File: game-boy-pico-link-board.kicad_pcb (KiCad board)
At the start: 2 copper layers, 83 x 26 mm, 6 parts, among them J1 GBA_Link, J2 GB_Link, J3 Breakout, SW1 SW_SPDT, U1 Pico, U2 BOB-12009

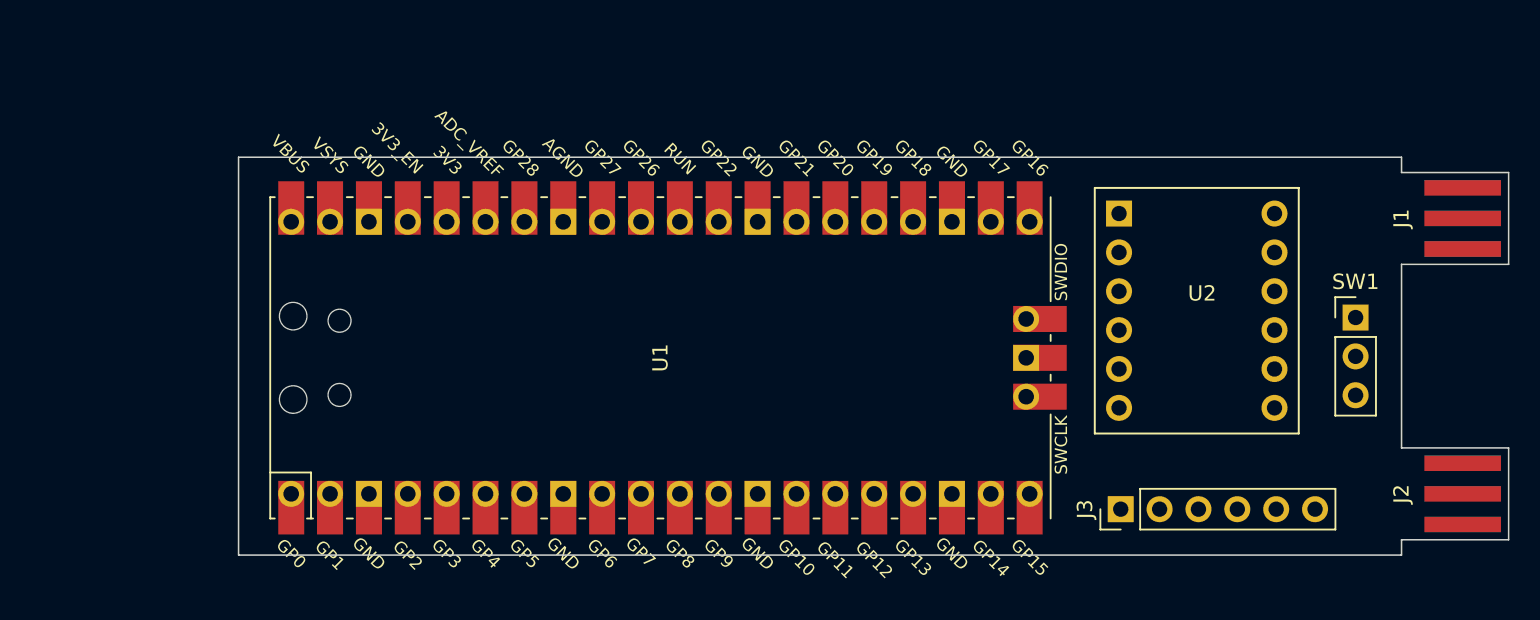
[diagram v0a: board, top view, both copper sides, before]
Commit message: Update Design and Add Routing
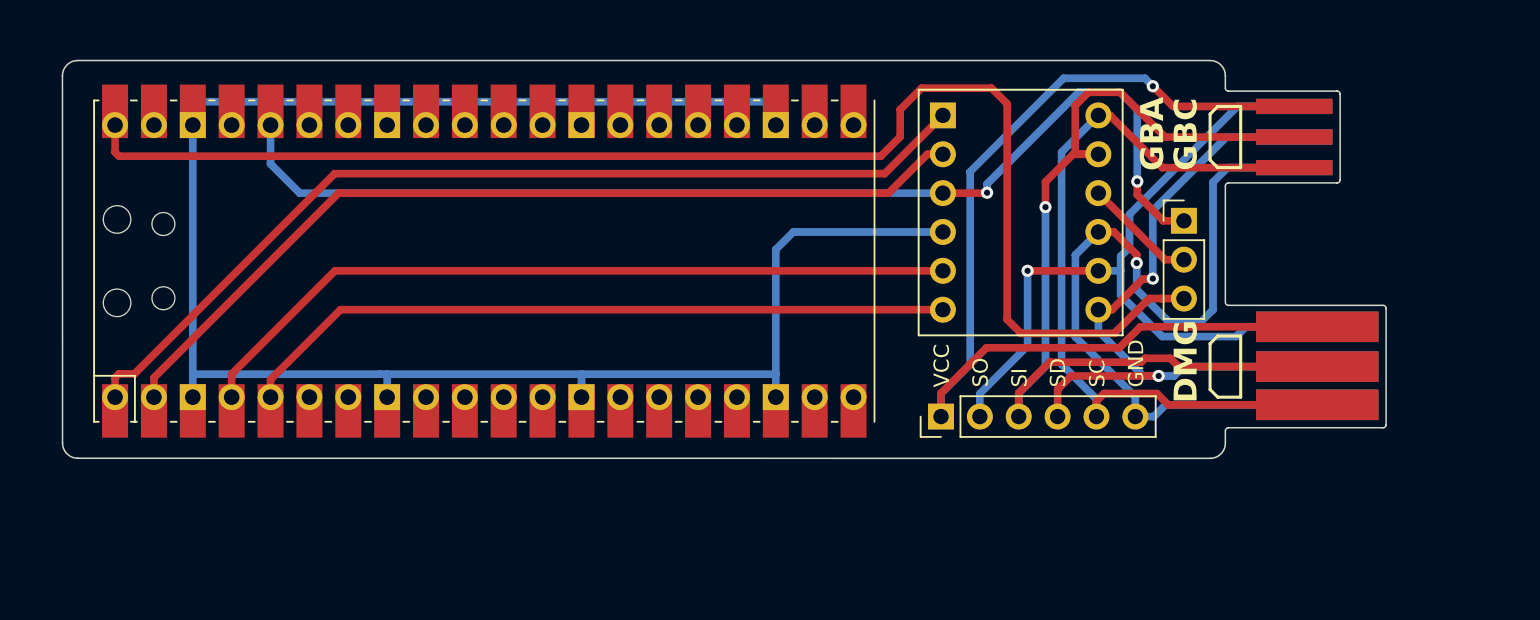
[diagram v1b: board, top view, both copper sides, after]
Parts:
- J1: moved to B.Cu
- J2: value GB_Link -> DMG_Link; footprint gb-link-socket:gb-link-socket -> gb-link-socket:dmg-link-socket; moved to B.Cu
- U1: value Pico -> Pico_Reduced; footprint MCU_RaspberryPi_and_Boards:RPi_Pico_SMD_TH -> MCU_RaspberryPi_and_Boards:RPi_Pico_SMD_TH_REDUCED
- moved J3 13.2 mm to (128.9, 108.0)
- moved U2 13.2 mm to (134.5, 94.6)
- moved U1 13.1 mm to (99.1, 97.8)
- moved SW1 12.9 mm to (144.8, 95.2)
- moved J2 12.6 mm to (153.5, 104.7)
- moved J1 12.2 mm to (152.0, 89.7)
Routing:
- net GND: track 0.00 -> 124.2 mm
- net +5V: track 0.00 -> 90.5 mm
- net +3.3V: track 0.00 -> 72.8 mm, vias 0 -> 2
- net /GBVCC: track 0.00 -> 69.2 mm, vias 0 -> 1
- net /SI: track 0.00 -> 63.0 mm, vias 0 -> 1
- net /PSC: track 0.00 -> 62.5 mm
- net /PSI: track 0.00 -> 58.9 mm
- net GND1: track 0.00 -> 52.2 mm, vias 0 -> 1
- net /SC: track 0.00 -> 51.8 mm
- net /PSO: track 0.00 -> 50.8 mm
- net /SO: track 0.00 -> 50.3 mm, vias 0 -> 1
- net /PSD: track 0.00 -> 47.0 mm
- net /SD: track 0.00 -> 46.0 mm, vias 0 -> 2
- net VCCLOGIC: track 0.00 -> 7.39 mm
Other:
- board size 83 x 26 mm -> 86.5 x 26 mm
- board text added: "DMG"
- board text added: "GBA"
- board text added: "GBC"
- board text added: "GND"
- board text added: "GP0 <-> SC GP1 <-> SI GP2 <-> SO GP3 <-> SD"
- board text added: "SC"
- board text added: "SD"
- board text added: "SI"
- board text added: "SO"
- board text added: "USB TO GAMEBOY LINK CABLE ADAPTER"
- board text added: "VCC"

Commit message: Update Design
Shortened DMG socket
Replace components layout
Add more silkscreen text
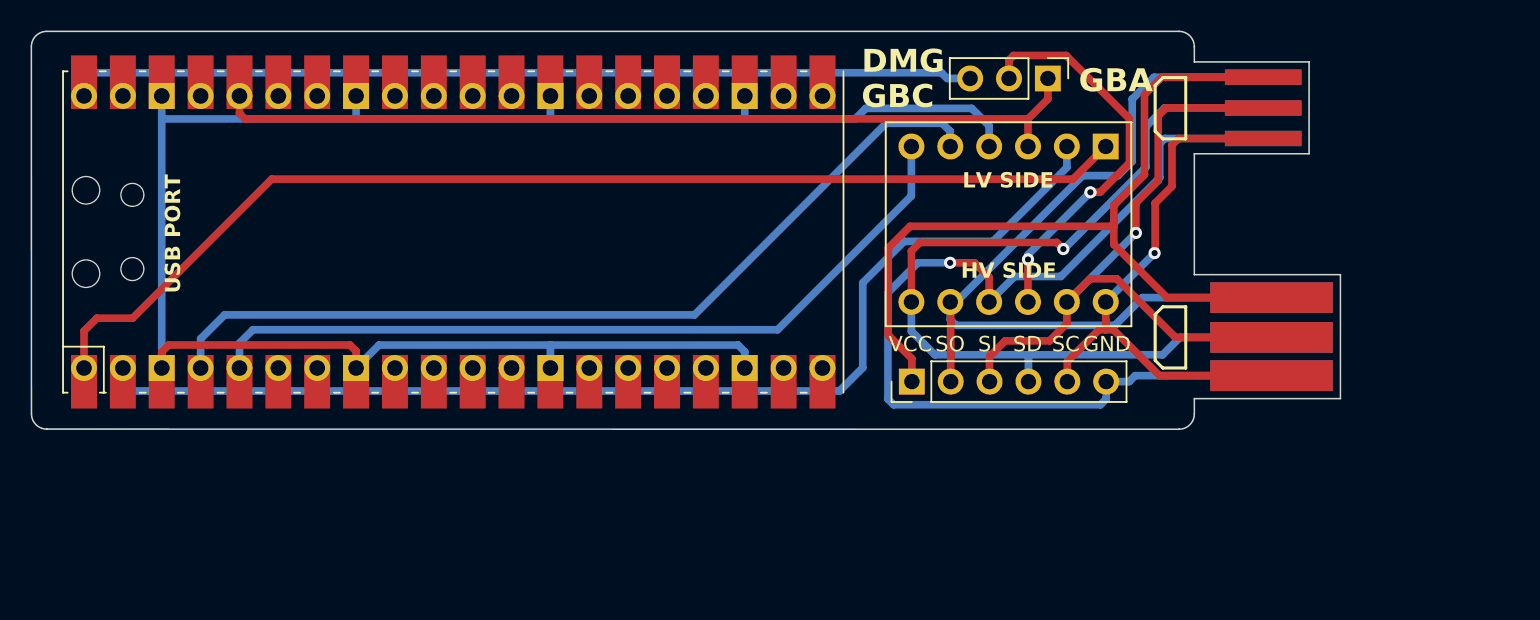
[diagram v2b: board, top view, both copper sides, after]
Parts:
- moved SW1 12.9 mm to (135.9, 85.9), turned to -90 degrees
- moved J2 3.54 mm to (150.5, 102.8)
- moved J3 2.98 mm to (127.0, 105.7)
- moved J1 2.78 mm to (150.0, 87.8)
- moved U1 2.78 mm to (97.0, 95.9)
- moved U2 1.64 mm to (133.3, 95.8), turned to -90 degrees
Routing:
- net +5V: track 90.5 -> 59.4 mm
- net VCCLOGIC: track 7.39 -> 26.0 mm, vias 0 -> 2
- net /SI: track 63.0 -> 46.3 mm
- net +3.3V: track 72.8 -> 57.8 mm, vias 2 -> 0
- net /SC: track 51.8 -> 36.8 mm, vias 0 -> 1
- net /PSI: track 58.9 -> 73.6 mm
- net GND1: track 52.2 -> 66.7 mm
- net /SD: track 46.0 -> 60.4 mm, vias 2 -> 1
- net /GBVCC: track 69.2 -> 55.3 mm, vias 1 -> 0
- net /PSC: track 62.5 -> 74.2 mm
- net /PSO: track 50.8 -> 57.9 mm
- net /SO: track 50.3 -> 57.3 mm, vias 1 -> 0
- net /PSD: track 47.0 -> 52.8 mm
- net GND: track 124.2 -> 122.4 mm
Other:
- board size 86.5 x 26 mm -> 85.5 x 26 mm
- board text added: "HV SIDE"
- board text added: "LV SIDE"
- board text added: "USB PORT"
- board text added: "agtbaskara.com"
- board text added: "version 1.0 2023"

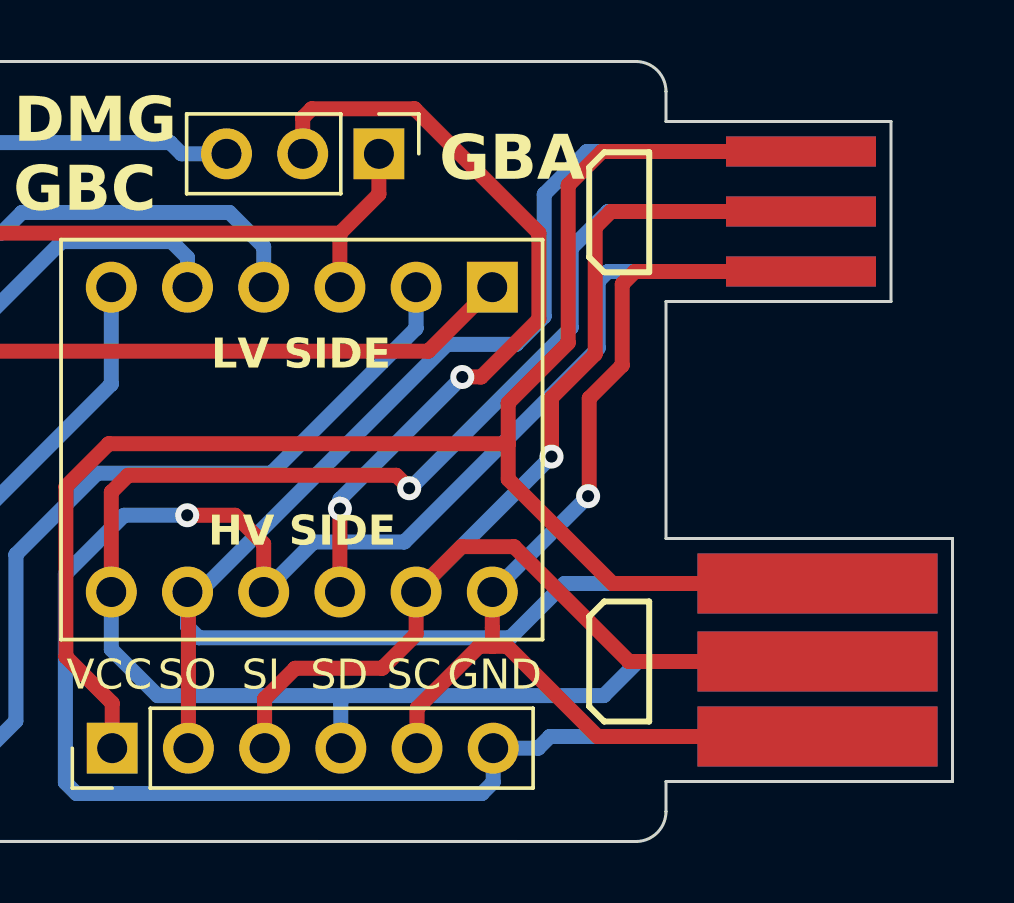
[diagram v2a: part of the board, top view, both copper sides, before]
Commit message: Update Connector Size
Add extra 0.5mm padding on the connector width
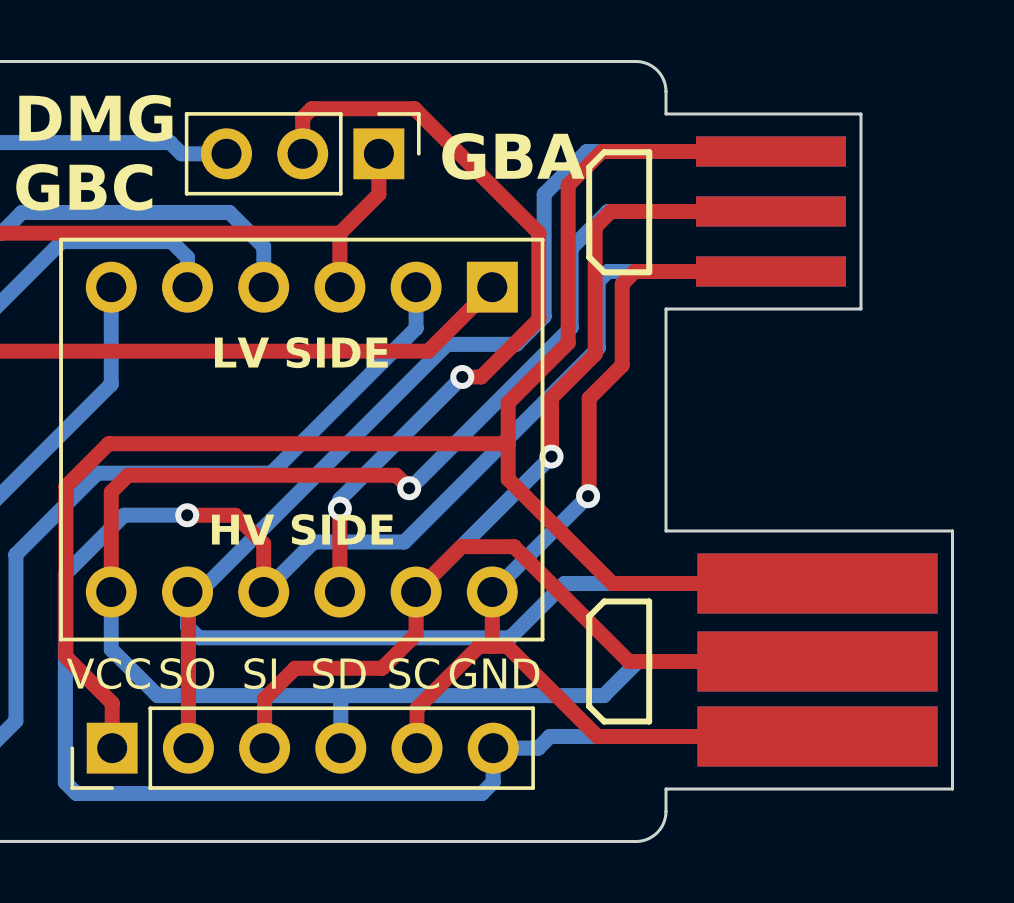
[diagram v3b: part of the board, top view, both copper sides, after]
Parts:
- moved J1 1.00 mm to (149.0, 87.8)
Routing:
- net /SC: track 36.8 -> 35.8 mm
- net GND1: track 66.7 -> 65.7 mm
- net /SO: track 57.3 -> 56.3 mm
- net /SI: track 46.3 -> 45.3 mm
- net /GBVCC: track 55.3 -> 54.3 mm
- net /SD: track 60.4 -> 59.4 mm
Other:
- outline, holes or cut-outs redrawn
- board text added: "version 1.5 2023"
- board text removed: "version 1.0 2023"
